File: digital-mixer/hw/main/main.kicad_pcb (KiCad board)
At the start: 2 copper layers, 104.5 x 136.5 mm, 190 parts, among them J1 GCT USB4110-GF-A, J10 MIDI OUT SJ-43514-SMT, J2 LiPo 1S 3000 mAh (з платою за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, J3 IN1 SJ-43514-SMT, J4 IN2 SJ-43514-SMT, J5 IN3 SJ-43514-SMT, J6 IN4 SJ-43514-SMT, J7 MAIN OUT SJ-43514-SMT, J8 AUX OUT SJ-43514-SMT, J9 PHONES SJ-43514-SMT, Q1 AO3401A, SW1 Power 5.8mm DPDT self-lock SMD, SW10 EC12SY ch3.1, SW11 EC12SY ch3.2, SW12 EC12SY ch3.3, SW13 Mute 3 TSF-1266, SW14 EC12SY ch4.1, SW15 EC12SY ch4.2, SW16 EC12SY ch4.3, SW17 Mute 4 TSF-1266, SW18 EC12SY master, SW19 FX1 TSF-1266, SW2 EC12SY ch1.1, SW20 FX2 TSF-1266, SW21 AUX TSF-1266, SW22 SHIFT TSF-1266, SW3 EC12SY ch1.2, SW4 EC12SY ch1.3, SW5 Mute 1 TSF-1266, SW6 EC12SY ch2.1, SW7 EC12SY ch2.2, SW8 EC12SY ch2.3, SW9 Mute 2 TSF-1266, U1 Teensy 4.1, U10 PCM5102A, U11 TPA6132A2, U12 MCP23017-E/SO, U13 MCP23017-E/SO, U14 MCP23017-E/SO, U2 USBLC6-2SC6, U3 TP4056, U4 TPS63802, U5 LP5907MFX-3.3, U6 PCM1865, U7 PCM1865, U8 PCM5102A, U9 PCM5102A

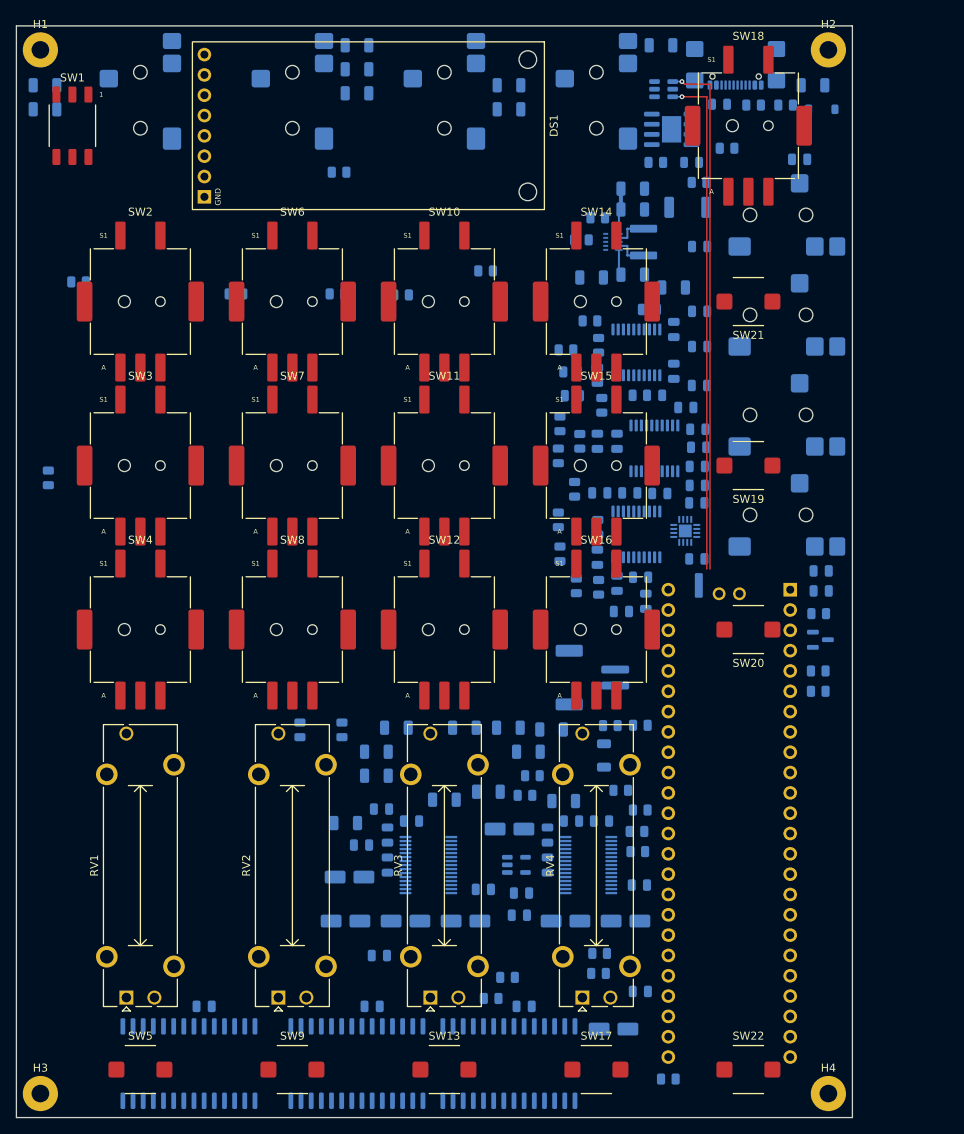
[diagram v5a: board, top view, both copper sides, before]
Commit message: digital-mixer: фейдери Alps RS201111J011 замість Bourns PTA2043 (DM39)
Footprint і 3D-модель за кресленням № 1 каталогу Alps (і продавця): 3 виводи Ø1,5,
25 і 3,75 мм. Центр ходу на старому місці; на розведеній платі R12/R13/R48 зсунуто,
38 з'єднань проведено заново. ERC 0, DRC 0 порушень, 0 розривів, 0 розбіжностей.

Co-Authored-By: Claude Opus 5.5 <noreply@anthropic.com>
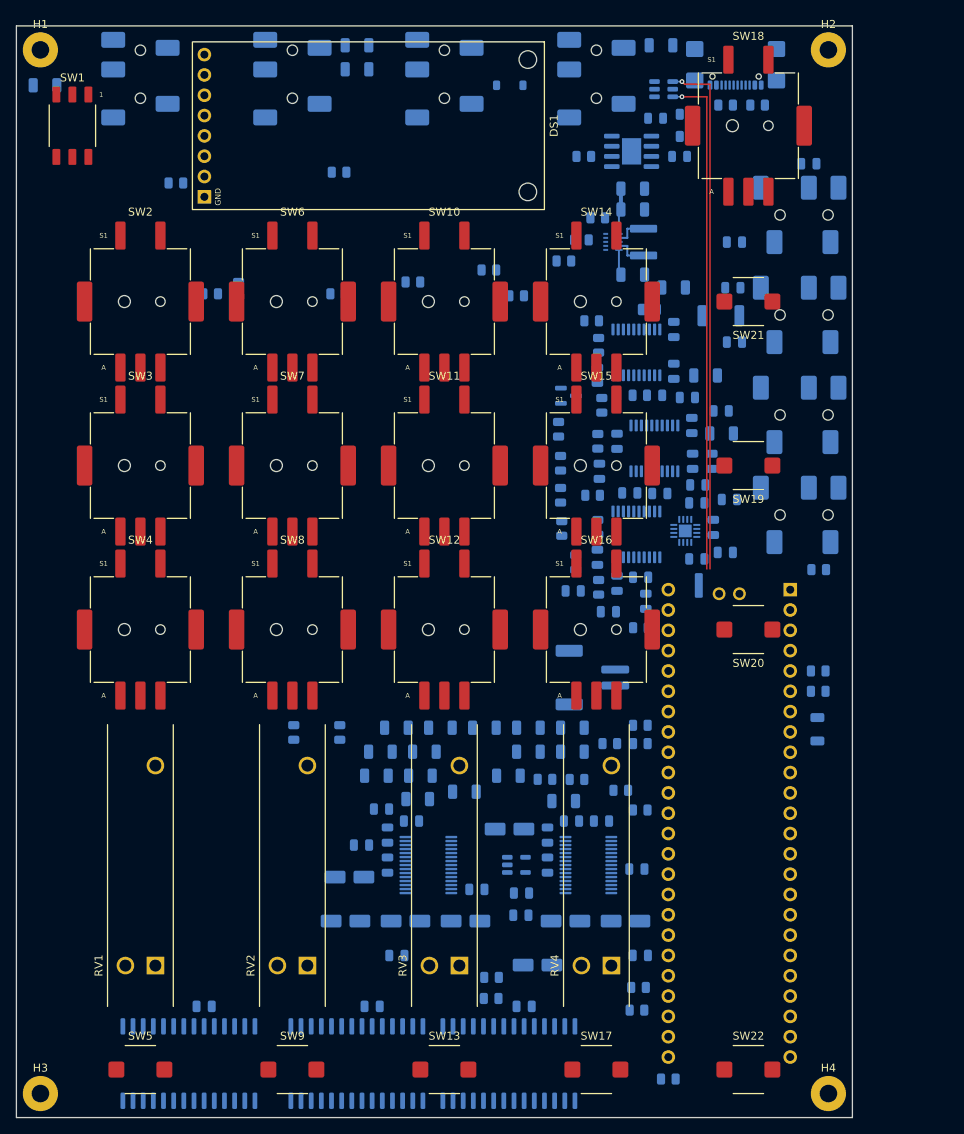
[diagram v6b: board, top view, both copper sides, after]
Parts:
- C11: value 10u -> 2.2u
- C18, C30, C41, C52, C63: value 10u -> 1u
- J10: value MIDI OUT SJ-43514-SMT -> MIDI OUT PJ-327A; footprint pocket-digital:CUI_SJ-43514-SMT_TRRS_Horizontal -> pocket-digital:Jack_3.5mm_PJ-327A_SMT_Horizontal
- J3: value IN1 SJ-43514-SMT -> IN1 PJ-327A; footprint pocket-digital:CUI_SJ-43514-SMT_TRRS_Horizontal -> pocket-digital:Jack_3.5mm_PJ-327A_SMT_Horizontal
- J4: value IN2 SJ-43514-SMT -> IN2 PJ-327A; footprint pocket-digital:CUI_SJ-43514-SMT_TRRS_Horizontal -> pocket-digital:Jack_3.5mm_PJ-327A_SMT_Horizontal
- J5: value IN3 SJ-43514-SMT -> IN3 PJ-327A; footprint pocket-digital:CUI_SJ-43514-SMT_TRRS_Horizontal -> pocket-digital:Jack_3.5mm_PJ-327A_SMT_Horizontal
- J6: value IN4 SJ-43514-SMT -> IN4 PJ-327A; footprint pocket-digital:CUI_SJ-43514-SMT_TRRS_Horizontal -> pocket-digital:Jack_3.5mm_PJ-327A_SMT_Horizontal
- J7: value MAIN OUT SJ-43514-SMT -> MAIN OUT PJ-327A; footprint pocket-digital:CUI_SJ-43514-SMT_TRRS_Horizontal -> pocket-digital:Jack_3.5mm_PJ-327A_SMT_Horizontal
- J8: value AUX OUT SJ-43514-SMT -> AUX OUT PJ-327A; footprint pocket-digital:CUI_SJ-43514-SMT_TRRS_Horizontal -> pocket-digital:Jack_3.5mm_PJ-327A_SMT_Horizontal
- J9: value PHONES SJ-43514-SMT -> PHONES PJ-327A; footprint pocket-digital:CUI_SJ-43514-SMT_TRRS_Horizontal -> pocket-digital:Jack_3.5mm_PJ-327A_SMT_Horizontal
- RV1, RV2, RV3, RV4: value PTA2043 10k B -> RS201111J011 10k B; footprint Potentiometer_THT:Potentiometer_Bourns_PTA2043_Single_Slide -> pocket-digital:Potentiometer_Alps_RS20111_Single_Slide
- moved C42 96.5 mm to (76.0, 115.7)
- moved C52 93.3 mm to (65.5, 110.7)
- moved C5 88.7 mm to (70.5, 113.7)
- moved C53 87.9 mm to (65.0, 113.7)
- moved C41 85.4 mm to (67.5, 107.7)
- moved C82 58.1 mm to (23.6, 27.4)
- moved C6 57.2 mm to (62.6, 22.4)
- moved Q1 43.8 mm to (89.0, 66.2)
- moved C66 42.7 mm to (108.2, 71.0)
- moved C64 39.3 mm to (62.6, 25.4)
- moved D3 39.1 mm to (81.7, 27.4)
- moved C63 38.5 mm to (100.6, 22.4)
- moved R26 33.5 mm to (47.8, 52.9)
- moved C68 31.0 mm to (89.6, 90.6)
- moved C27 28.2 mm to (81.6, 120.4)
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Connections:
- J10 pad 2: /MIDI_SINK -> /GND
- J10 pad 4: /GND -> /MIDI_SINK
- J3 pad 2: /IN1_T -> /GND
- J3 pad 4: /GND -> /IN1_T
- J4 pad 2: /IN2_T -> /GND
- J4 pad 4: /GND -> /IN2_T
- J5 pad 2: /IN3_T -> /GND
- J5 pad 4: /GND -> /IN3_T
- J6 pad 2: /IN4_T -> /GND
- J6 pad 4: /GND -> /IN4_T
- J7 pad 2: /MAIN_L -> /GND
- J7 pad 4: /GND -> /MAIN_L
- J8 pad 2: /AUX_L -> /GND
- J8 pad 4: /GND -> /AUX_L
- J9 pad 2: /PH_L -> /GND
- J9 pad 4: /GND -> /PH_L
